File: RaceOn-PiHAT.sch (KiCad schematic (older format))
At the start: 60 parts, among them IC1 SPX29302T5, IC2 NCP5901B, IC3 BD48K60G, IC4 NCP5901B, IC5 LMR14030, J1 Conn_01x02, J2 Battery, J3 Servo_motor, J4 Conn_02x20_Odd_Even, J5 Accelerometer_standard, M1 Motor_Servo, M2 Mabuchi 540, Q1 Si7288DP, Q2 Si7288DP, Q3 SQJA37EP1

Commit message: Included all parts in the schematic
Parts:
- removed C12: 10uF, library_express_pro:RLC_EIA_3216, symbol Device:C
- removed J1: Conn_01x02, library_express_pro:Connector_pads, symbol Connector_Generic:Conn_01x02
- removed J3: Servo_motor, library_express_pro:servo_connector, symbol Connector_Generic:Conn_01x03
- removed JP1: SolderJumper_3_Bridged12, Jumper:SolderJumper-3_P1.3mm_Open_RoundedPad1.0x1.5mm_NumberLabels, symbol Jumper:SolderJumper_3_Bridged12
- added J?: Encoder Left, symbol Connector_Generic:Conn_01x03
- added J?: Encoder Right, symbol Connector_Generic:Conn_01x03
- added JP?: SolderJumper, symbol RaceOn-PiHAT:SolderJumper
- added TP?: TestPoint, symbol Connector:TestPoint
- M1: value Motor_Servo -> Servo
- S?: renamed from Btn1; value PTS636 -> LEFT
- S?: renamed from Btn2; value PTS636 -> RIGHT
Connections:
- net labels added: +3V3, BCM0, BCM1, BCM10, BCM11, BCM12, BCM13, BCM14, BCM15, BCM16, BCM17, BCM18, BCM19, BCM2, BCM20, BCM21, BCM22, BCM23, BCM24, BCM25, BCM26, BCM27, BCM3, BCM4, BCM5, BCM6, BCM7, BCM8, BCM9
- net labels removed: GPIO12, GPIO16, GPIO20, GPIO21, GPIO25, GPIO26, GPIO5, GPIO6, GPIO8, SCL, SDA, Vservo
- wire segments 223 -> 230
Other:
- note added: "Accelerometer"
- note added: "Connectors"
- note added: "Mounting Holes"
- note added: "Reverse Battery Protection"
- note added: "Sides are fliped as connector\nis mounted on the back\n\nCheck https://pinout.xyz/\nfor additional details\n"
- note added: "TO DO: Reasign signals to components"
- note added: "User Controls"
- note added: "Wheel Encoders"
- moved on the sheet: C3, C4, H1, H2, H3, H4, IC3, J2, J4, LED1, LED2, LED3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

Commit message: Assign OPL number to each part to be assembled
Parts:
- removed C1, C6: 100nF, Pi HAT Footprints:CAPC320X160X180L50M, symbol Device:C
- removed C10, C3, C4, C9: 1uF, Pi HAT Footprints:CAPC320X160X180L50M, symbol Device:C
- removed C2, C7: 47nF, Pi HAT Footprints:CAPC320X160X180L50M, symbol Device:C
- removed IC2: NCP5901B, symbol RaceOn-PiHAT:NCP5901B
- removed LED3, LED4: 599-0210-007F, library_express_pro:RLC_EIA_3216, symbol Device:LED
- removed Q1: Si7288DP, symbol RaceOn-PiHAT:Si7288DP
- removed unit 1 of Q2
- removed R10, R3: 2.2k, library_express_pro:RLC_EIA_3216, symbol Device:R
- removed R11: 6.8k, library_express_pro:RLC_EIA_3216, symbol Device:R
- removed R2, R6: 1k, library_express_pro:RLC_EIA_3216, symbol Device:R
- removed R4: 22.1k, library_express_pro:RLC_EIA_3216, symbol Device:R
- added C?: 47uF, Pi HAT Footprints:CAPC320X250X180L50L, symbol Device:C
- added C? (x2): 47nF, symbol Device:C
- added C? (x2): 100nF, symbol Device:C
- added C? (x2): 4.7uF, symbol Device:C
- added C? (x2): 1uF, symbol Device:C
- added IC?: NCP5901B, symbol RaceOn-PiHAT:NCP5901B
- added LED?: RED, symbol Device:LED
- added LED?: GREEN, symbol Device:LED
- added Q? (x3): Si7288DP, symbol RaceOn-PiHAT:Si7288DP
- added R? (x4): 12.1k, symbol Device:R
- added R? (x3): 4.7k, symbol Device:R
- added TP?: TestPoint, symbol Connector:TestPoint
- C11: MPN (none) -> TAJD107K010RNJ
- C13: footprint Pi HAT Footprints:CAPC320X160X180L50M -> (none); MPN (none) -> GCM21BR72A104KA37L
- C14: value 1uF -> 4.7uF; footprint Pi HAT Footprints:CAPC320X160X180L50M -> (none); MPN (none) -> CL31A475KOHNNNE
- C15: value 22uF -> 47uF; MPN (none) -> EMK325BJ476MM-T
- C16: value 100nF -> 47nF; footprint Pi HAT Footprints:CAPC320X160X180L50M -> (none); MPN (none) -> CL21B473KBCNNNC
- C5: footprint Pi HAT Footprints:CAPC320X160X180L50M -> (none); MPN (none) -> 0805B273K500CT
- C8: footprint Pi HAT Footprints:CAPC320X160X180L50M -> (none); MPN (none) -> CL21B105KBFNNNE
- D1: MPN (none) -> MBRS540T3G
- IC1: MPN (none) -> SPX29302T5-L/TR
- IC3, IC4, LS1, M2: MPN (none) -> NOT IN OPL
- IC5: MPN (none) -> LMR14030SDDAR
- J4: footprint library_express_pro:RasPi_Header_0.9 -> (none); MPN (none) -> PF1-M220-SBB-G0-TR
- L1: value 3.3uH -> 1uH; footprint Pi HAT Footprints:INDC800X800X450L240M -> (none); MPN (none) -> WPN4020H1R0MT
- LED1: value 599-0210-007F -> GREEN; footprint library_express_pro:RLC_EIA_3216 -> (none); MPN (none) -> ORH-YG35A
- LED2: value 599-0210-007F -> RED; footprint library_express_pro:RLC_EIA_3216 -> (none); MPN (none) -> ORH-R35A
- M1: MPN (none) -> A2543WR-3P-2
- Q2: MPN (none) -> SI7288DP-T1-GE3
- Q3: footprint library_express_pro:SO-8L -> (none); MPN (none) -> IRF9310TRPBF
- R1: value 66.3k -> 46.4k; footprint library_express_pro:RLC_EIA_3216 -> (none); MPN (none) -> 0805W8F4642T5E
- R5: value 2.2k -> 4.7k; footprint library_express_pro:RLC_EIA_3216 -> (none); MPN (none) -> 0805W8J0472T5E
- R7: value 124k -> 68.1k; footprint library_express_pro:RLC_EIA_3216 -> (none); MPN (none) -> 0805W8F6812T5E
- R8: value 11k -> 12.1k; footprint library_express_pro:RLC_EIA_3216 -> (none); MPN (none) -> 0805W8F1212T5E
- R9: value 22.1k -> 12.1k; footprint library_express_pro:RLC_EIA_3216 -> (none); MPN (none) -> 0805W8F1212T5E
- S? (x2): MPN (none) -> K2-1102SP-C4SC-04
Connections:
- net labels removed: GPIO13, GPIO18, GPIO23, GPIO24
- wire segments 230 -> 236
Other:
- note added: "Create footprints for parts\nTruth table on how to controll motor"
- note added: "Create footprints\nDescribe output performance"
- note added: "Create footprints\nRoute this part\n"
- note added: "Disable the Drivers"
- note removed: "Calculate components value\nSelect Components from the OPL\nCreate footprints\nRoute this part\nDescribe output performance"
- note removed: "Choose better pins for inputs\nSelect capacitors from the OPL\nCreate footprints for capacitors\nRoute this part\nTruth table on how to controll motor"
- note removed: "Select components from the OPL\nCreate footprints\nRoute this part\n"
- note removed: "TO DO: Reasign signals to components"
- moved on the sheet: C11, C13, C14, C15, C16, D1, IC5, J2, J5, L1, LED1, Q3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

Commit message: Add footprints for all parts
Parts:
- removed IC1: SPX29302T5, symbol RaceOn-PiHAT:SPX29302T5
- added D1: D_Schottky, Race On:DIOM795X590X261L117X305M, symbol Device:D_Schottky
- added FID1: Fiducial, Race On:FID1M3, symbol Mechanical:Fiducial
- added IC1: MIC29302WU, Race On:DPAK6P67_587X190L89X29T300X275M, symbol RaceOn-PiHAT:MIC29302WU
- C1, C2, C4, C6, C7, C9: renamed from C?; footprint (none) -> Race On:CAPC200X125X95L45M
- C10, C3: renamed from C?; footprint (none) -> Race On:CAPC320X160X180L50M
- C11: footprint (none) -> Race On:CAPPM730X435X310L135X240L
- C12: renamed from C13; footprint (none) -> Race On:CAPC200X125X95L45M
- C13: renamed from C14; footprint (none) -> Race On:CAPC320X160X180L50M
- C14: renamed from C15; footprint Pi HAT Footprints:CAPC320X250X180L50L -> Race On:CAPC320X250X270L60M
- C15: renamed from C?; footprint Pi HAT Footprints:CAPC320X250X180L50L -> Race On:CAPC320X250X270L60M
- C16, C5, C8: footprint (none) -> Race On:CAPC200X125X95L45M
- D2: renamed from D1; footprint (none) -> Race On:DIOM795X590X261L117X305M
- H1, H2, H3, H4: footprint MountingHole:MountingHole_2.7mm_M2.5 -> Race On:MTGP620H275V8H50
- IC2: renamed from IC?; footprint (none) -> Race On:SOIC8P127_490X600X175L83X42M
- IC3: renamed from IC4; footprint (none) -> Race On:SOIC8P127_490X600X175L83X42M
- IC4: renamed from IC3; footprint (none) -> Race On:SOT23-3P95_280X125L45X40M
- IC5: footprint (none) -> Race On:SOIC9P127_490X600X170L83X41T287X202M
- J1: renamed from J2; footprint library_express_pro:Connector_pads -> Race On:CON2P
- J2: renamed from J5; value Accelerometer_standard -> Accelerometer; footprint library_express_pro:Accelerometer_standard -> Race On:HDRV4W64P254_4X1_1016X254H854
- J3: renamed from J4; value Conn_02x20_Odd_Even -> Pi Connector; footprint (none) -> Race On:RHDRV40W64P254_20X2_5120X500H850
- J4, J5: renamed from J?; footprint (none) -> Race On:HDRV3W64P254_3X1_762X254H854
- JP1: renamed from JP?; footprint (none) -> Race On:SJ3B12P10X15
- L1: footprint (none) -> Race On:INDM400X400X200L95X310M
- LED1: renamed from LED2; footprint (none) -> Race On:LEDC197X125X85L45L
- LED2: renamed from LED1; footprint (none) -> Race On:LEDC197X125X85L45L
- LED3, LED4: renamed from LED?; footprint (none) -> Race On:LEDC197X125X85L45L
- LS1: footprint library_express_pro:Buzzer_AI1027TWT5V2R -> Race On:LSP500W60D980H500
- M1: footprint (none) -> Race On:HDRV3W64P254_3X1_762X254H854
- M2: footprint (none) -> Race On:CON2P
- Q1, Q2: renamed from Q?; footprint (none) -> Race On:ICSOFL8P127_515X615X112L61X42M
- Q2: footprint (none) -> Race On:ICSOFL8P127_515X615X112L61X42M
- Q3: footprint (none) -> Race On:SOIC8P127_490X600X175L83X42M-TRANZISTOR
- R1, R5: footprint (none) -> Race On:RESC200X127X65L40M
- R10: renamed from R9; footprint (none) -> Race On:RESC200X127X65L40M
- R11, R12, R2, R3, R4, R6, R7: renamed from R?; footprint (none) -> Race On:RESC200X127X65L40M
- R8: renamed from R7; footprint (none) -> Race On:RESC200X127X65L40M
- R9: renamed from R8; footprint (none) -> Race On:RESC200X127X65L40M
- S1, S2: renamed from S?; footprint library_express_pro:PTS636 -> Race On:BTN4P450_600X900X350L83X70M
- TP1: renamed from TP2; footprint (none) -> Race On:TESTPOINT
- TP2: renamed from TP1; footprint (none) -> Race On:TESTPOINT
- TP3, TP6: renamed from TP?; footprint (none) -> Race On:TESTPOINT
- TP4: renamed from TP3; footprint (none) -> Race On:TESTPOINT
- TP5: renamed from TP4; footprint (none) -> Race On:TESTPOINT
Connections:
- wire segments 236 -> 238

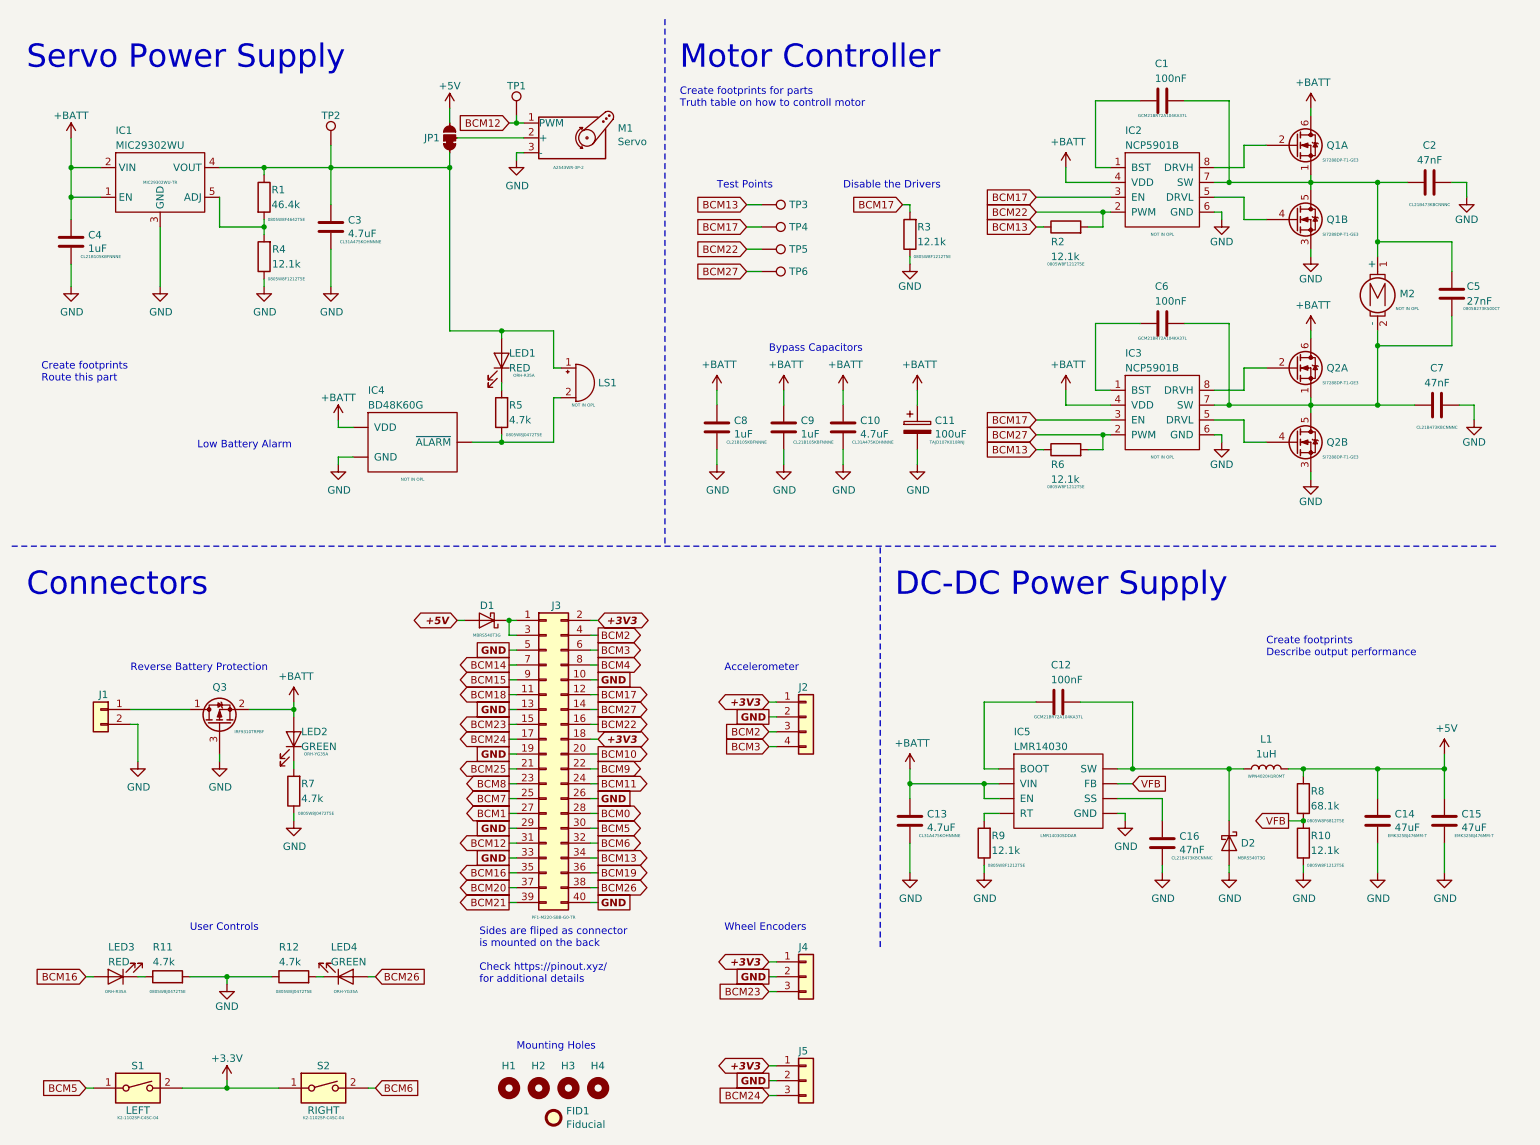
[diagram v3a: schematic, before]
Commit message: Ordered from Seeed PCBA
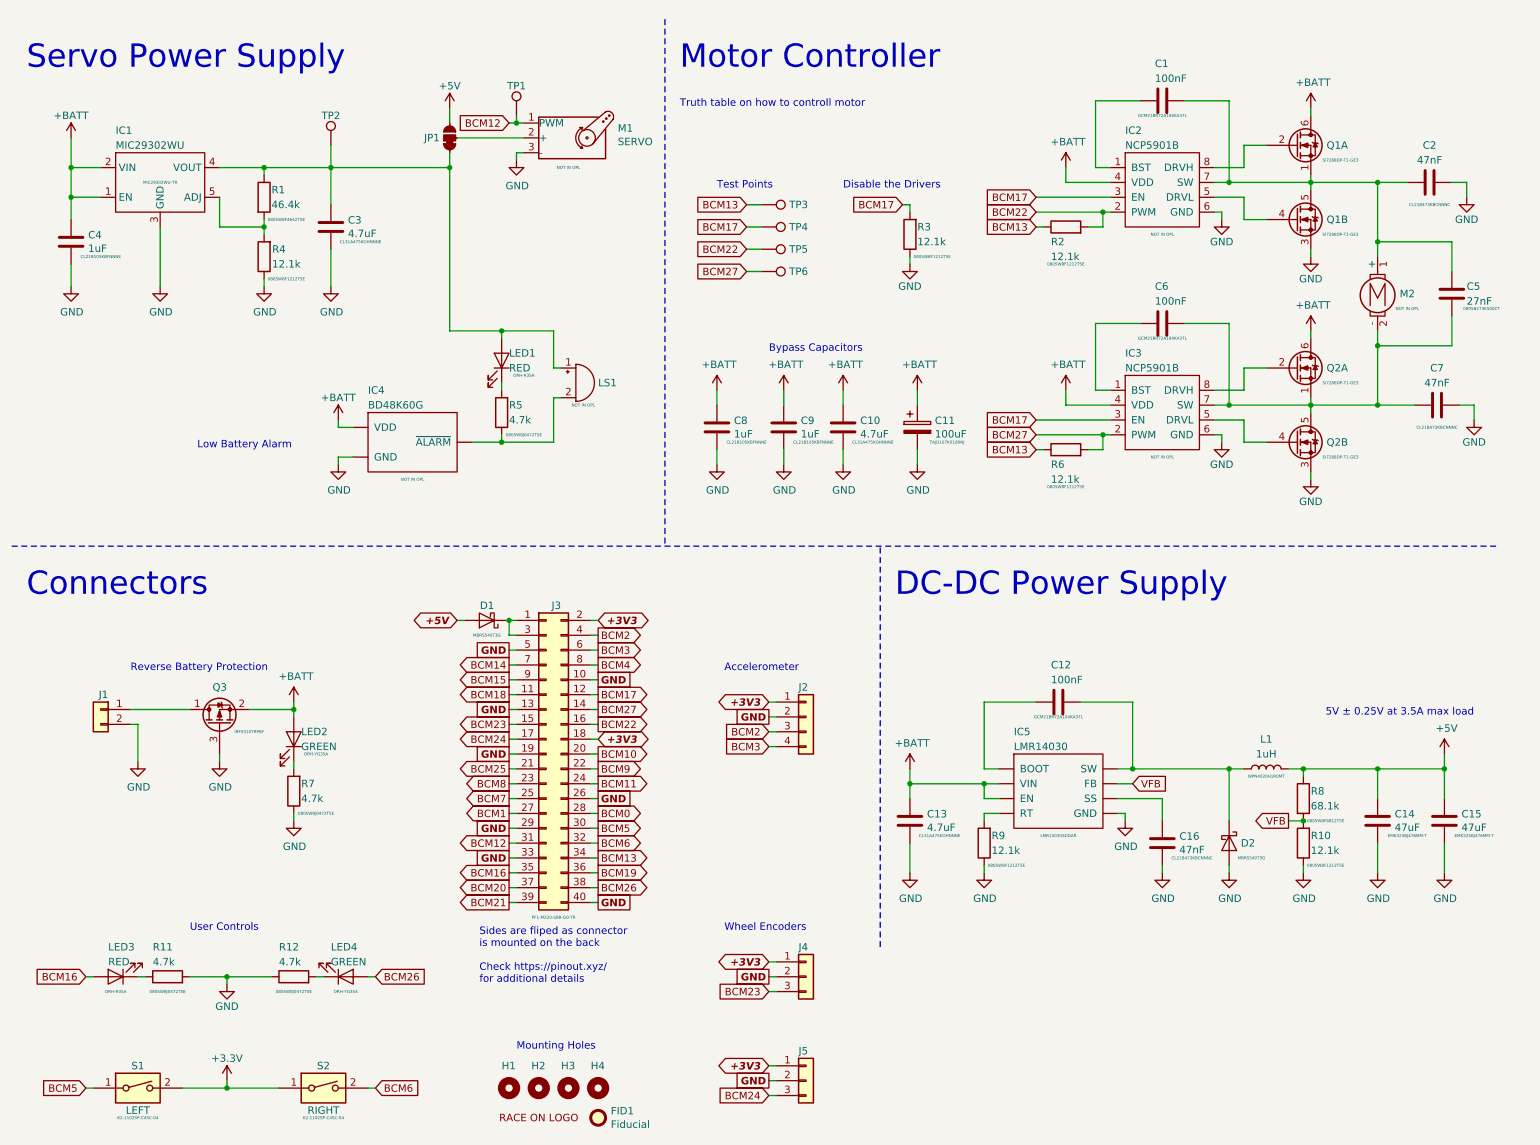
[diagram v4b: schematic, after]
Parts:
- added LOGO1: RACEON-LOGO, Race On:RACEON-LOGO, symbol RaceOn-PiHAT:RACEON-LOGO
- J1: value Battery -> BATTERY
- J2: value Accelerometer -> ACCELEROMETER
- M1: value Servo -> SERVO; MPN A2543WR-3P-2 -> NOT IN OPL
- M2: value Mabuchi 540 -> MOTOR
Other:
- note added: "5V ± 0.25V at 3.5A max load"
- note added: "Truth table on how to controll motor"
- note removed: "Create footprints for parts\nTruth table on how to controll motor"
- note removed: "Create footprints\nDescribe output performance"
- note removed: "Create footprints\nRoute this part\n"
- moved on the sheet: FID1
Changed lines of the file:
@@
 Sheet 1 1
 Title "Race On – Pi HAT"
-Date "2019-08-12"
+Date "2019-08-15"
 Rev "1"
 Comp "University of Southern California"
@@
 Comment2 "sponsored by"
 Comment3 ""
-Comment4 "Race On - A Self-Driving Car Competition                             http://raceon.com/"
+Comment4 "Race On - A Self-Driving Car Competition                                http://raceon.io/"
 $EndDescr
 $Comp
@@
 P 1050 5150
 F 0 "J1" H 1000 5250 50  0000 L CNN
-F 1 "Battery" H 1130 5051 50  0001 L CNN
+F 1 "BATTERY" H 1130 5051 50  0001 L CNN
 F 2 "Race On:CON2P" H 1050 5150 50  0001 C CNN
 F 3 "~" H 1050 5150 50  0001 C CNN
@@
 P 5800 5200
 F 0 "J2" H 5750 5400 50  0000 L CNN
-F 1 "Accelerometer" H 5880 5146 50  0001 L CNN
+F 1 "ACCELEROMETER" H 5880 5146 50  0001 L CNN
 F 2 "Race On:HDRV4W64P254_4X1_1016X254H854" H 5800 5200 50  0001 C CNN
 F 3 "~" H 5800 5200 50  0001 C CNN
@@
 	2550 6950 2500 6950
 Text Notes 4950 1100 0    50   ~ 0
-Create footprints for parts\nTruth table on how to controll motor
+Truth table on how to controll motor
 $Comp
 L Motor:Motor_Servo M1
@@
 P 4200 1300
 F 0 "M1" H 4532 1365 50  0000 L CNN
-F 1 "Servo" H 4532 1274 50  0000 L CNN
+F 1 "SERVO" H 4532 1274 50  0000 L CNN
 F 2 "Race On:HDRV3W64P254_3X1_762X254H854" H 4200 1110 50  0001 C CNN
 F 3 "" H 4200 1110 50  0001 C CNN
-F 4 "A2543WR-3P-2" H 4200 1100 20  0000 C CNN "MPN"
+F 4 "NOT IN OPL" H 4200 1100 20  0000 C CNN "MPN"
 	1    4200 1300
 	1    0    0    -1
@@
 P 9650 2300
 F 0 "M2" H 9850 2250 50  0000 C CNN
-F 1 "Mabuchi 540" V 9843 2250 50  0001 C CNN
+F 1 "MOTOR" V 9843 2250 50  0001 C CNN
 F 2 "Race On:CON2P" H 9650 2210 50  0001 C CNN
 F 3 "" H 9650 2210 50  0001 C CNN
@@
 	6500 5750 6500 5650
 Connection ~ 6500 5650
-Text Notes 8900 4800 0    50   ~ 0
-Create footprints\nDescribe output performance
+Text Notes 9300 5200 0    50   ~ 0
+5V ± 0.25V at 3.5A max load
 $Comp
 L Connector_Generic:Conn_02x20_Odd_Even J3
@@
 Wire Wire Line
 	2600 1350 2600 1500
-Text Notes 650  2950 0    50   ~ 0
-Create footprints\nRoute this part\n
 $Comp
 L Device:R R5
@@
 L Mechanical:Fiducial FID1
 U 1 1 5D55ABFE
-P 4100 7900
-F 0 "FID1" H 4185 7946 50  0000 L CNN
-F 1 "Fiducial" H 4185 7855 50  0000 L CNN
-F 2 "Race On:FID1M3" H 4100 7900 50  0001 C CNN
-F 3 "~" H 4100 7900 50  0001 C CNN
-	1    4100 7900
+P 4400 7900
+F 0 "FID1" H 4485 7946 50  0000 L CNN
+F 1 "Fiducial" H 4485 7855 50  0000 L CNN
+F 2 "Race On:FID1M3" H 4400 7900 50  0001 C CNN
+F 3 "~" H 4400 7900 50  0001 C CNN
+	1    4400 7900
 	1    0    0    -1
 $EndComp
@@
 	0    1    -1   0
 $EndComp
+$Comp
+L RaceOn-PiHAT:RACEON-LOGO LOGO1
+U 1 1 5D55E528
+P 4000 7900
+F 0 "LOGO1" H 4000 7900 50  0001 C CNN
+F 1 "RACEON-LOGO" H 4000 7900 50  0001 C CNN
+F 2 "Race On:RACEON-LOGO" H 4000 7900 50  0001 C CNN
+F 3 "" H 4000 7900 50  0001 C CNN
+	1    4000 7900
+	1    0    0    -1
+$EndComp
 $EndSCHEMATC
